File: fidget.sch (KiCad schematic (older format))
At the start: 89 parts, among them J1 KEYSTONE 120, J2 KEYSTONE 120, Q1 PEMZ7, U1 MCP73831-2ACI/MC, U2 ESP8285, U3 TLV70033DSE, U4 LIS2DE, U5 TPS60150, U6 TPS60150, U7 TPS60150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

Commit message: PCB design at 4am.. probably a bad idea
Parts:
- removed TP3: RST, Measurement_Points:Measurement_Point_Round-SMD-Pad_Small, symbol TEST
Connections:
- wire segments 279 -> 278
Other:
- moved on the sheet: R10
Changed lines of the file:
@@
 	0    1    1    0
 $EndComp
-$Comp
-L TEST TP3
-U 1 1 593A6F8C
-P 4600 2700
-F 0 "TP3" H 4600 3000 50  0000 C BNN
-F 1 "RST" H 4600 2950 50  0000 C CNN
-F 2 "Measurement_Points:Measurement_Point_Round-SMD-Pad_Small" H 4600 2700 50  0001 C CNN
-F 3 "" H 4600 2700 50  0001 C CNN
-	1    4600 2700
-	0    -1   -1   0
-$EndComp
-Wire Wire Line
-	4600 2500 4600 2700
 Wire Wire Line
 	4600 2600 4900 2600
@@
 L R R10
 U 1 1 593A7228
-P 4450 2500
-F 0 "R10" V 4530 2500 50  0000 C CNN
-F 1 "12k" V 4450 2500 50  0000 C CNN
-F 2 "Resistors_SMD:R_0402" V 4380 2500 50  0001 C CNN
-F 3 "" H 4450 2500 50  0001 C CNN
-	1    4450 2500
+P 4450 2600
+F 0 "R10" V 4530 2600 50  0000 C CNN
+F 1 "12k" V 4450 2600 50  0000 C CNN
+F 2 "Resistors_SMD:R_0402" V 4380 2600 50  0001 C CNN
+F 3 "" H 4450 2600 50  0001 C CNN
+	1    4450 2600
 	0    1    1    0
 $EndComp
-Connection ~ 4600 2600
 $Comp
 L +3V3 #PWR35
 U 1 1 593A74E3
-P 4300 2500
-F 0 "#PWR35" H 4300 2350 50  0001 C CNN
-F 1 "+3V3" H 4300 2640 50  0000 C CNN
-F 2 "" H 4300 2500 50  0001 C CNN
-F 3 "" H 4300 2500 50  0001 C CNN
-	1    4300 2500
+P 4300 2600
+F 0 "#PWR35" H 4300 2450 50  0001 C CNN
+F 1 "+3V3" H 4300 2740 50  0000 C CNN
+F 2 "" H 4300 2600 50  0001 C CNN
+F 3 "" H 4300 2600 50  0001 C CNN
+	1    4300 2600
 	1    0    0    -1
 $EndComp
@@
 Text Label 4650 1900 0    60   ~ 0
 IDX
-Text Label 1500 3700 0    60   ~ 0
-LCK
-Text Label 1500 3900 0    60   ~ 0
-LSO
-$Comp
-L R R8
-U 1 1 593A930F
-P 1850 3700
-F 0 "R8" V 1930 3700 50  0000 C CNN
-F 1 "NC" V 1850 3700 50  0000 C CNN
-F 2 "Resistors_SMD:R_0402" V 1780 3700 50  0001 C CNN
-F 3 "" H 1850 3700 50  0001 C CNN
-	1    1850 3700
-	0    1    1    0
-$EndComp
-$Comp
-L R R9
-U 1 1 593A94C5
-P 1850 3900
-F 0 "R9" V 1930 3900 50  0000 C CNN
-F 1 "NC" V 1850 3900 50  0000 C CNN
-F 2 "Resistors_SMD:R_0402" V 1780 3900 50  0001 C CNN
-F 3 "" H 1850 3900 50  0001 C CNN
-	1    1850 3900
-	0    1    1    0
-$EndComp
-Wire Wire Line
-	1700 3700 1500 3700
-Wire Wire Line
-	1500 3900 1700 3900
-$Comp
-L +5C #PWR16
-U 1 1 593A9A2E
-P 2100 3600
-F 0 "#PWR16" H 2100 3450 50  0001 C CNN
-F 1 "+5C" H 2100 3740 50  0000 C CNN
-F 2 "" H 2100 3600 50  0001 C CNN
-F 3 "" H 2100 3600 50  0001 C CNN
-	1    2100 3600
-	1    0    0    -1
-$EndComp
-Wire Wire Line
-	2100 3700 2000 3700
-Wire Wire Line
-	2100 3600 2100 3900
-Wire Wire Line
-	2100 3900 2000 3900
-Connection ~ 2100 3700
 $Comp
 L +5C #PWR8
@@
 	1    0    0    -1
 $EndComp
+Wire Wire Line
+	1700 3700 1500 3700
+Text Label 1500 3700 0    60   ~ 0
+LCK
+Wire Wire Line
+	1500 3900 1700 3900
+Text Label 1500 3900 0    60   ~ 0
+LSO
+Wire Wire Line
+	2100 3900 2000 3900
+$Comp
+L +5C #PWR16
+U 1 1 593A9A2E
+P 2100 3600
+F 0 "#PWR16" H 2100 3450 50  0001 C CNN
+F 1 "+5C" H 2100 3740 50  0000 C CNN
+F 2 "" H 2100 3600 50  0001 C CNN
+F 3 "" H 2100 3600 50  0001 C CNN
+	1    2100 3600
+	1    0    0    -1
+$EndComp
+Connection ~ 2100 3700
+Wire Wire Line
+	2100 3600 2100 3900
+Wire Wire Line
+	2100 3700 2000 3700
+$Comp
+L R R8
+U 1 1 593A930F
+P 1850 3700
+F 0 "R8" V 1930 3700 50  0000 C CNN
+F 1 "NC" V 1850 3700 50  0000 C CNN
+F 2 "Resistors_SMD:R_0402" V 1780 3700 50  0001 C CNN
+F 3 "" H 1850 3700 50  0001 C CNN
+	1    1850 3700
+	0    1    1    0
+$EndComp
+$Comp
+L R R9
+U 1 1 593A94C5
+P 1850 3900
+F 0 "R9" V 1930 3900 50  0000 C CNN
+F 1 "NC" V 1850 3900 50  0000 C CNN
+F 2 "Resistors_SMD:R_0402" V 1780 3900 50  0001 C CNN
+F 3 "" H 1850 3900 50  0001 C CNN
+	1    1850 3900
+	0    1    1    0
+$EndComp
 $EndSCHEMATC

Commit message: RTFM: reverse polarity protection is already inside MCP73831
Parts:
- removed Q1: PEMZ7, TO_SOT_Packages_SMD:SOT-666, symbol Q_DUAL_NPN_PNP_E1B1C2E2B2C1
- removed R13, R4: 2k, Resistors_SMD:R_0402, symbol R
- removed R8, R9: NC, Resistors_SMD:R_0402, symbol R
- C6: value 12p -> 10p
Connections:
- wire segments 278 -> 358
- no-connect marks 16 -> 13

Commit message: routing done
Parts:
- added TP3: GND, Measurement_Points:Measurement_Point_Round-SMD-Pad_Small, symbol TEST
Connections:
- net GND: now also TP3.1

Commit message: cleaned up silkscreen
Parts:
- added G1: HACKADAY, parts:wrencher_8mm, symbol OPEN_HARDWARE_1
- added G2: OPEN_HARDWARE, Symbols:OSHW-Logo_7.5x8mm_SilkScreen, symbol OPEN_HARDWARE_1
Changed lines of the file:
@@
 LIBS:Worldsemi
 LIBS:switches
+LIBS:logo
 LIBS:fidget-cache
 EELAYER 25 0
@@
 	-1   0    0    -1
 $EndComp
+$Comp
+L OPEN_HARDWARE_1 G2
+U 1 1 593C1D56
+P 10850 6200
+F 0 "G2" H 10850 6475 50  0000 C CNN
+F 1 "OPEN_HARDWARE" H 10850 5975 50  0000 C CNN
+F 2 "Symbols:OSHW-Logo_7.5x8mm_SilkScreen" H 10850 6200 50  0001 C CNN
+F 3 "" H 10850 6200 50  0001 C CNN
+	1    10850 6200
+	1    0    0    -1
+$EndComp
+$Comp
+L OPEN_HARDWARE_1 G1
+U 1 1 593C230C
+P 10300 6200
+F 0 "G1" H 10300 6475 50  0000 C CNN
+F 1 "HACKADAY" H 10300 5975 50  0000 C CNN
+F 2 "parts:wrencher_8mm" H 10300 6200 50  0001 C CNN
+F 3 "" H 10300 6200 50  0001 C CNN
+	1    10300 6200
+	1    0    0    -1
+$EndComp
 $EndSCHEMATC

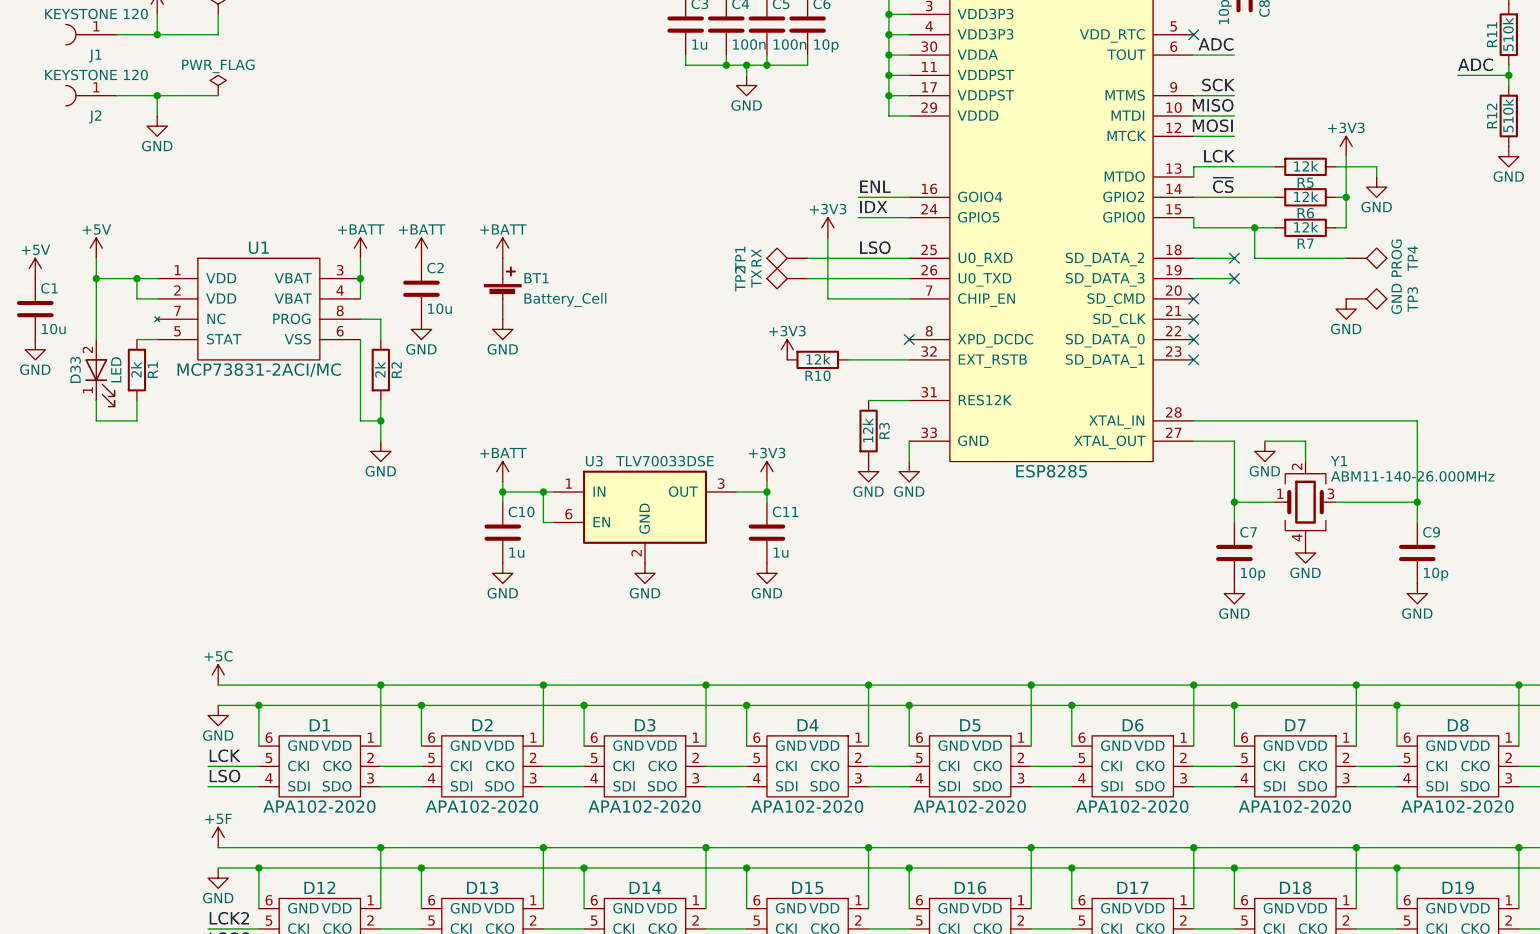
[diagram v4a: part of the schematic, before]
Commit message: added level shifter
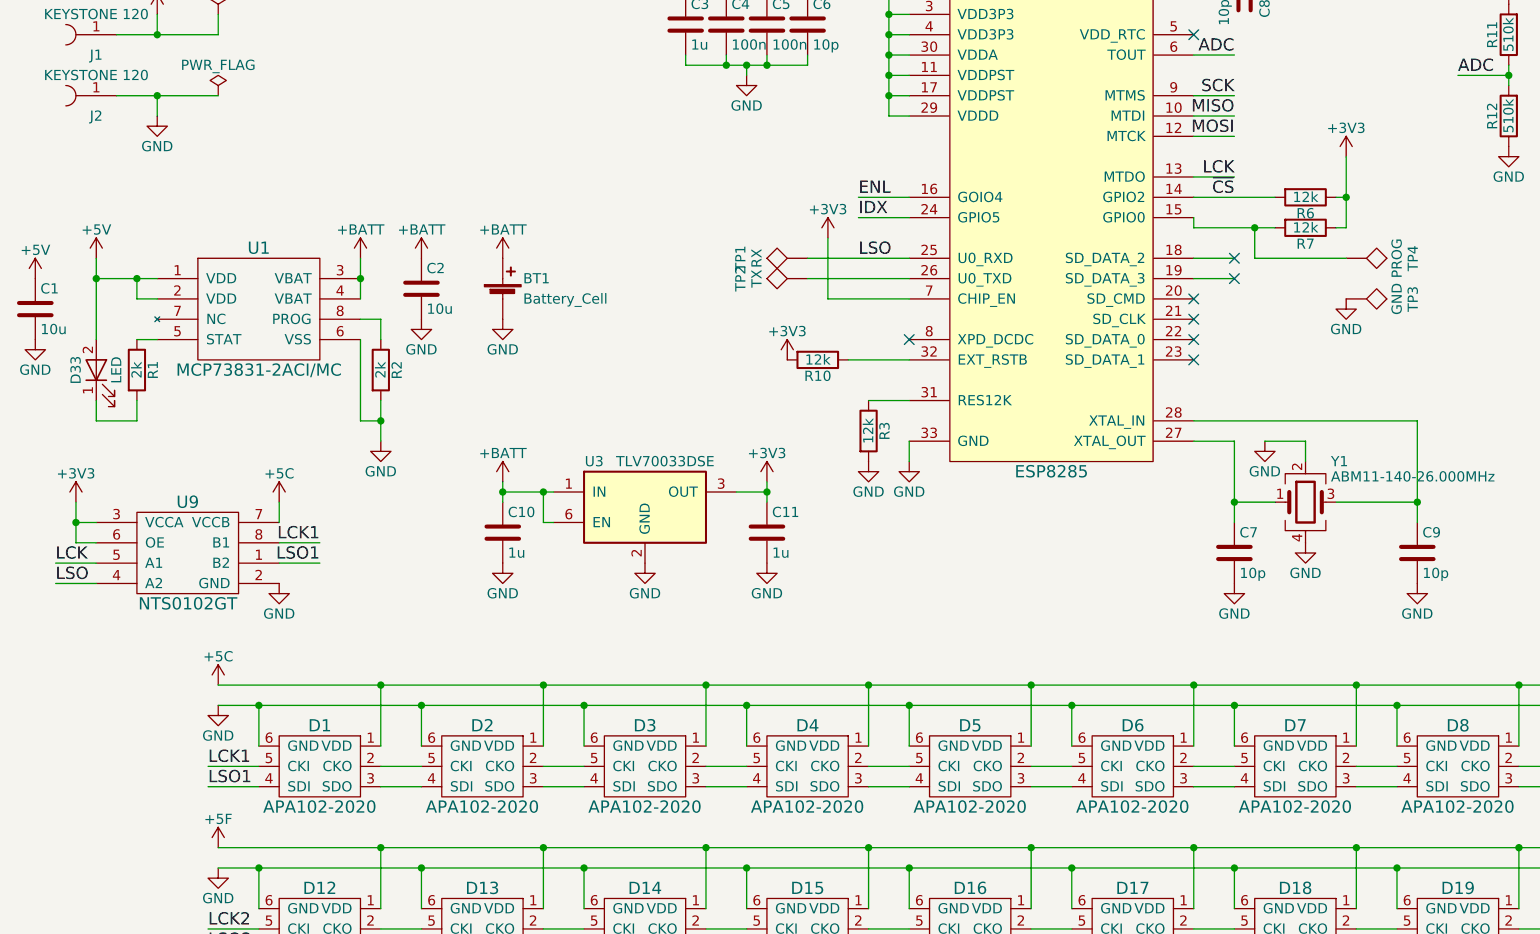
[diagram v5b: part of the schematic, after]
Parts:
- removed R5: 12k, Resistors_SMD:R_0402, symbol R
- added U9: NTS0102GT, parts:SOT833-1, symbol NTS0102GT
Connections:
- net +3V3: now also U9.3 (VCCA), U9.6 (OE)
- net +5C: now also U9.7 (VCCB)
- net GND: now also U9.2 (GND)
- net LCK: now also U9.5 (A1); no longer D1.5 (CKI)
- net LSO: now also U9.4 (A2); no longer D1.4 (SDI)
- new net LCK1: D1.5 (CKI), U9.8 (B1)
- new net LSO1: D1.4 (SDI), U9.1 (B2)

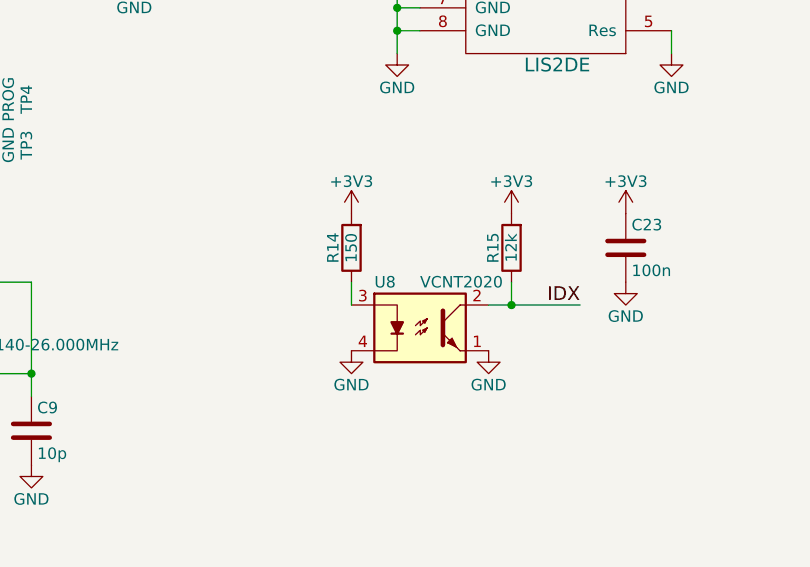
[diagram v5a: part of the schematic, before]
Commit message: switched to hall sensor
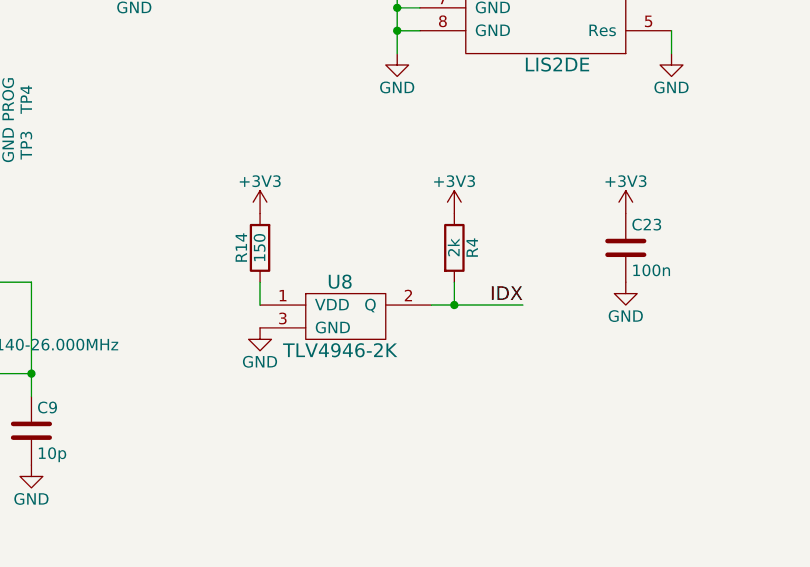
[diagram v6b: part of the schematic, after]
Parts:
- removed R15: 12k, Resistors_SMD:R_0402, symbol R
- removed U8: VCNT2020, parts:VCNT2020, symbol VCNT2020
- added R4: 2k, Resistors_SMD:R_0402, symbol R
- added U8: TLV4946-2K, TO_SOT_Packages_SMD:SC-59, symbol TLV4946-2K
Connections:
- net +3V3: now also R4.1
- net GND: now also U8.3 (GND)
- net IDX: now also R4.2, U8.2 (Q)
- net at R14.1: now also U8.1 (VDD)
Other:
- moved on the sheet: R14
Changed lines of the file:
@@
 $EndComp
 $Comp
-L GND #PWR54
+L GND #PWR53
 U 1 1 593915EC
 P 7400 3700
-F 0 "#PWR54" H 7400 3450 50  0001 C CNN
+F 0 "#PWR53" H 7400 3450 50  0001 C CNN
 F 1 "GND" H 7400 3550 50  0000 C CNN
 F 2 "" H 7400 3700 50  0001 C CNN
@@
 Connection ~ 7850 1200
 $Comp
-L GND #PWR56
+L GND #PWR55
 U 1 1 593AD258
 P 7850 1550
-F 0 "#PWR56" H 7850 1300 50  0001 C CNN
+F 0 "#PWR55" H 7850 1300 50  0001 C CNN
 F 1 "GND" H 7850 1400 50  0000 C CNN
 F 2 "" H 7850 1550 50  0001 C CNN
@@
 $EndComp
 $Comp
-L +BATT #PWR55
+L +BATT #PWR54
 U 1 1 593AD6A9
 P 7850 850
-F 0 "#PWR55" H 7850 700 50  0001 C CNN
+F 0 "#PWR54" H 7850 700 50  0001 C CNN
 F 1 "+BATT" H 7850 990 50  0000 C CNN
 F 2 "" H 7850 850 50  0001 C CNN
@@
 	9100 1400 8800 1400
 $Comp
-L GND #PWR59
+L GND #PWR58
 U 1 1 593D3B49
 P 9000 1900
-F 0 "#PWR59" H 9000 1650 50  0001 C CNN
+F 0 "#PWR58" H 9000 1650 50  0001 C CNN
 F 1 "GND" H 9000 1750 50  0000 C CNN
 F 2 "" H 9000 1900 50  0001 C CNN
@@
 $EndComp
 $Comp
-L +3V3 #PWR65
+L +3V3 #PWR63
 U 1 1 593D54E3
 P 10300 1000
-F 0 "#PWR65" H 10300 850 50  0001 C CNN
+F 0 "#PWR63" H 10300 850 50  0001 C CNN
 F 1 "+3V3" H 10300 1140 50  0000 C CNN
 F 2 "" H 10300 1000 50  0001 C CNN
@@
 $EndComp
 $Comp
-L +3V3 #PWR66
+L +3V3 #PWR64
 U 1 1 593D5595
 P 10600 1000
-F 0 "#PWR66" H 10600 850 50  0001 C CNN
+F 0 "#PWR64" H 10600 850 50  0001 C CNN
 F 1 "+3V3" H 10600 1140 50  0000 C CNN
 F 2 "" H 10600 1000 50  0001 C CNN
@@
 $EndComp
 $Comp
-L +3V3 #PWR68
+L +3V3 #PWR66
 U 1 1 593D5647
 P 10900 1000
-F 0 "#PWR68" H 10900 850 50  0001 C CNN
+F 0 "#PWR66" H 10900 850 50  0001 C CNN
 F 1 "+3V3" H 10900 1140 50  0000 C CNN
 F 2 "" H 10900 1000 50  0001 C CNN
@@
 NoConn ~ 10200 1500
 $Comp
-L GND #PWR64
+L GND #PWR62
 U 1 1 593D5C8D
 P 10200 1900
-F 0 "#PWR64" H 10200 1650 50  0001 C CNN
+F 0 "#PWR62" H 10200 1650 50  0001 C CNN
 F 1 "GND" H 10200 1750 50  0000 C CNN
 F 2 "" H 10200 1900 50  0001 C CNN
@@
 	10200 1900 10200 1800
 $Comp
-L GND #PWR67
+L GND #PWR65
 U 1 1 593D6080
 P 10600 1300
-F 0 "#PWR67" H 10600 1050 50  0001 C CNN
+F 0 "#PWR65" H 10600 1050 50  0001 C CNN
 F 1 "GND" H 10600 1150 50  0000 C CNN
 F 2 "" H 10600 1300 50  0001 C CNN
@@
 $EndComp
 $Comp
-L GND #PWR69
+L GND #PWR67
 U 1 1 593D6132
 P 10900 1300
-F 0 "#PWR69" H 10900 1050 50  0001 C CNN
+F 0 "#PWR67" H 10900 1050 50  0001 C CNN
 F 1 "GND" H 10900 1150 50  0000 C CNN
 F 2 "" H 10900 1300 50  0001 C CNN
@@
 	1200 1400 1200 1300
 Connection ~ 1200 1300
-$Comp
-L VCNT2020 U8
-U 1 1 593B783F
-P 9100 3100
-F 0 "U8" H 8900 3300 50  0000 L CNN
-F 1 "VCNT2020" H 9100 3300 50  0000 L CNN
-F 2 "parts:VCNT2020" H 8900 2900 50  0001 L CIN
-F 3 "" H 9125 3100 50  0001 L CNN
-	1    9100 3100
-	1    0    0    -1
-$EndComp
-Text Label 9800 3000 2    60   ~ 0
+Text Label 9550 3000 2    60   ~ 0
 IDX
-$Comp
-L R R15
-U 1 1 593B900D
-P 9500 2750
-F 0 "R15" V 9580 2750 50  0000 C CNN
-F 1 "12k" V 9500 2750 50  0000 C CNN
-F 2 "Resistors_SMD:R_0402" V 9430 2750 50  0001 C CNN
-F 3 "" H 9500 2750 50  0001 C CNN
-	1    9500 2750
-	-1   0    0    1
-$EndComp
-Wire Wire Line
-	9500 2900 9500 3000
-Connection ~ 9500 3000
-Wire Wire Line
-	9400 3000 9800 3000
+Wire Wire Line
+	9250 2900 9250 3000
+Connection ~ 9250 3000
+Wire Wire Line
+	9150 3000 9550 3000
 $Comp
 L R R14
 U 1 1 593B9EB2
-P 8800 2750
-F 0 "R14" V 8880 2750 50  0000 C CNN
-F 1 "150" V 8800 2750 50  0000 C CNN
-F 2 "Resistors_SMD:R_0402" V 8730 2750 50  0001 C CNN
-F 3 "" H 8800 2750 50  0001 C CNN
-	1    8800 2750
+P 8400 2750
+F 0 "R14" V 8480 2750 50  0000 C CNN
+F 1 "150" V 8400 2750 50  0000 C CNN
+F 2 "Resistors_SMD:R_0402" V 8330 2750 50  0001 C CNN
+F 3 "" H 8400 2750 50  0001 C CNN
+	1    8400 2750
 	-1   0    0    1
 $EndComp
 Wire Wire Line
-	8800 2900 8800 3000
-$Comp
-L GND #PWR58
+	8400 2900 8400 3000
+$Comp
+L GND #PWR57
 U 1 1 593BA276
-P 8800 3200
-F 0 "#PWR58" H 8800 2950 50  0001 C CNN
-F 1 "GND" H 8800 3050 50  0000 C CNN
-F 2 "" H 8800 3200 50  0001 C CNN
-F 3 "" H 8800 3200 50  0001 C CNN
-	1    8800 3200
-	1    0    0    -1
-$EndComp
-$Comp
-L GND #PWR60
-U 1 1 593BA33C
-P 9400 3200
-F 0 "#PWR60" H 9400 2950 50  0001 C CNN
-F 1 "GND" H 9400 3050 50  0000 C CNN
-F 2 "" H 9400 3200 50  0001 C CNN
-F 3 "" H 9400 3200 50  0001 C CNN
-	1    9400 3200
-	1    0    0    -1
-$EndComp
-$Comp
-L +3V3 #PWR61
+P 8400 3100
+F 0 "#PWR57" H 8400 2850 50  0001 C CNN
+F 1 "GND" H 8400 2950 50  0000 C CNN
+F 2 "" H 8400 3100 50  0001 C CNN
+F 3 "" H 8400 3100 50  0001 C CNN
+	1    8400 3100
+	1    0    0    -1
+$EndComp
+$Comp
+L +3V3 #PWR59
 U 1 1 593BA402
-P 9500 2600
-F 0 "#PWR61" H 9500 2450 50  0001 C CNN
-F 1 "+3V3" H 9500 2740 50  0000 C CNN
-F 2 "" H 9500 2600 50  0001 C CNN
-F 3 "" H 9500 2600 50  0001 C CNN
-	1    9500 2600
-	1    0    0    -1
-$EndComp
-$Comp
-L +3V3 #PWR57
+P 9250 2600
+F 0 "#PWR59" H 9250 2450 50  0001 C CNN
+F 1 "+3V3" H 9250 2740 50  0000 C CNN
+F 2 "" H 9250 2600 50  0001 C CNN
+F 3 "" H 9250 2600 50  0001 C CNN
+	1    9250 2600
+	1    0    0    -1
+$EndComp
+$Comp
+L +3V3 #PWR56
 U 1 1 593BA4C8
-P 8800 2600
-F 0 "#PWR57" H 8800 2450 50  0001 C CNN
-F 1 "+3V3" H 8800 2740 50  0000 C CNN
-F 2 "" H 8800 2600 50  0001 C CNN
-F 3 "" H 8800 2600 50  0001 C CNN
-	1    8800 2600
+P 8400 2600
+F 0 "#PWR56" H 8400 2450 50  0001 C CNN
+F 1 "+3V3" H 8400 2740 50  0000 C CNN
+F 2 "" H 8400 2600 50  0001 C CNN
+F 3 "" H 8400 2600 50  0001 C CNN
+	1    8400 2600
 	1    0    0    -1
 $EndComp
@@
 $EndComp
 $Comp
-L +3V3 #PWR62
+L +3V3 #PWR60
 U 1 1 593C09A2
 P 10000 2600
-F 0 "#PWR62" H 10000 2450 50  0001 C CNN
+F 0 "#PWR60" H 10000 2450 50  0001 C CNN
 F 1 "+3V3" H 10000 2740 50  0000 C CNN
 F 2 "" H 10000 2600 50  0001 C CNN
@@
 $EndComp
 $Comp
-L GND #PWR63
+L GND #PWR61
 U 1 1 593C09A8
 P 10000 2900
-F 0 "#PWR63" H 10000 2650 50  0001 C CNN
+F 0 "#PWR61" H 10000 2650 50  0001 C CNN
 F 1 "GND" H 10000 2750 50  0000 C CNN
 F 2 "" H 10000 2900 50  0001 C CNN
@@
 Wire Wire Line
 	6300 1700 6500 1700
+$Comp
+L TLV4946-2K U8
+U 1 1 593F5A5E
+P 8750 3000
+F 0 "U8" H 8750 3100 60  0000 C CNN
+F 1 "TLV4946-2K" H 8750 2800 60  0000 C CNN
+F 2 "TO_SOT_Packages_SMD:SC-59" H 8750 3000 60  0001 C CNN
+F 3 "" H 8750 3000 60  0001 C CNN
+	1    8750 3000
+	1    0    0    -1
+$EndComp
+$Comp
+L R R4
+U 1 1 593F77B1
+P 9250 2750
+F 0 "R4" V 9330 2750 50  0000 C CNN
+F 1 "2k" V 9250 2750 50  0000 C CNN
+F 2 "Resistors_SMD:R_0402" V 9180 2750 50  0001 C CNN
+F 3 "" H 9250 2750 50  0001 C CNN
+	1    9250 2750
+	1    0    0    -1
+$EndComp
 $EndSCHEMATC
